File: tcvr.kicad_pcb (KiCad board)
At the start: 2 copper layers, 51 parts, among them J1 9V 43-04-70, J2 anterna 50 Ohm, J3 jack 43-08-39, J4 hole, Q1 BC817 86-05-47, Q2 2N7002, Q3 PZT2222A 86-02-43, SW1 SW_DPST_x2, U1 LM386 89-24-08, Y1 3579kHz 40-00-62

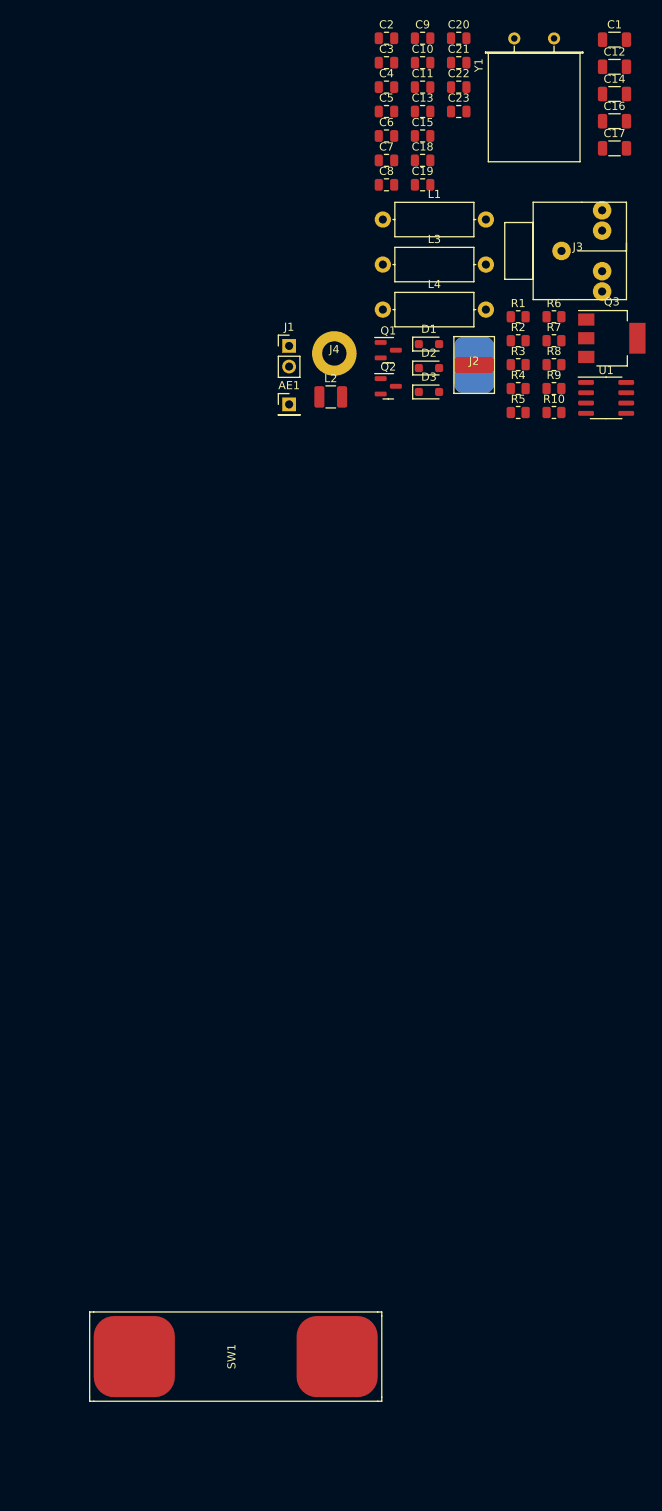
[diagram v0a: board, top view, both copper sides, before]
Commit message: made pcb placment
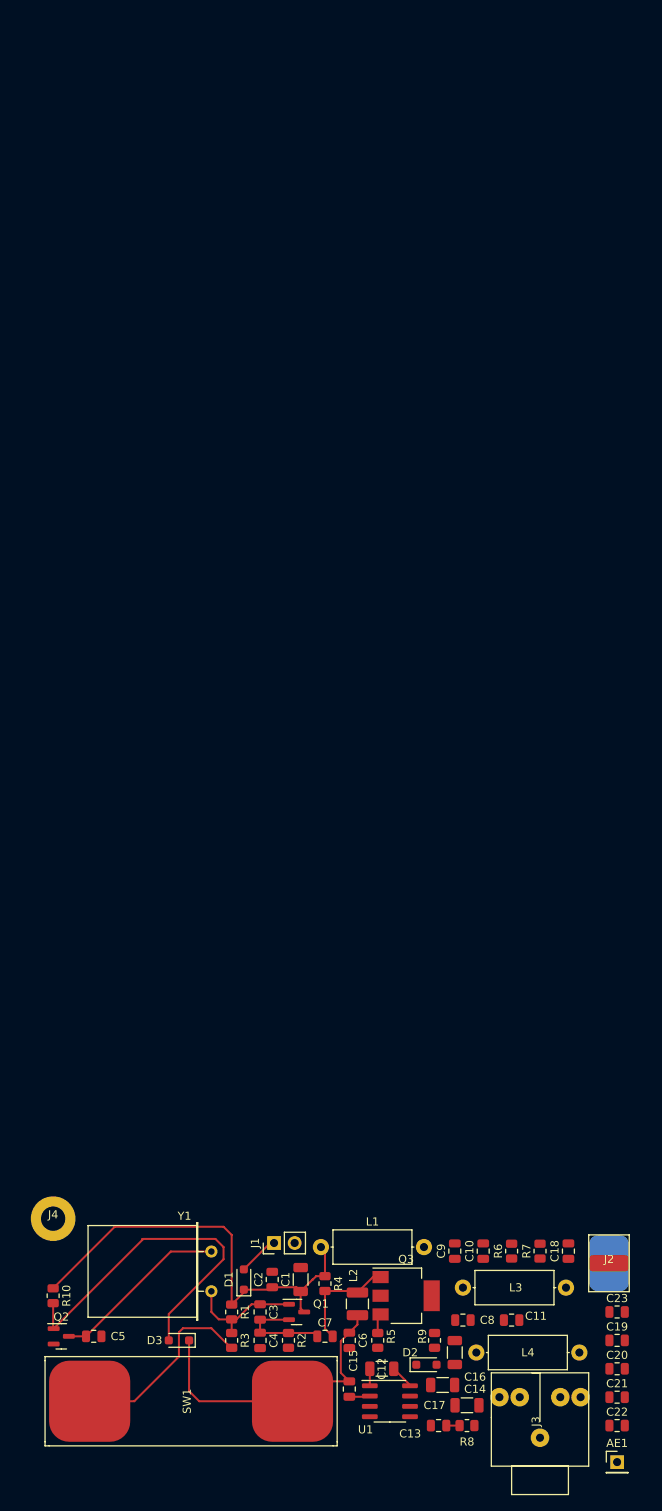
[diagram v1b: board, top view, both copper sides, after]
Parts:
- moved C22 166.1 mm to (147.5, 113.5)
- moved C21 165.6 mm to (147.5, 110.0)
- moved C20 165.1 mm to (147.5, 106.5)
- moved C12 163.0 mm to (118.5, 106.5), turned to 180 degrees
- moved C13 162.0 mm to (125.5, 113.5)
- moved C14 160.5 mm to (126.0, 108.5)
- moved C1 157.6 mm to (108.5, 95.5), turned to 90 degrees
- moved C17 156.0 mm to (129.0, 111.0)
- moved C4 155.2 mm to (103.5, 103.0), turned to -90 degrees
- moved C5 155.2 mm to (83.0, 102.5)
- moved C3 154.7 mm to (103.5, 99.5), turned to -90 degrees
- moved C15 154.7 mm to (114.5, 109.0), turned to 90 degrees
- moved Y1 154.1 mm to (97.5, 92.0), turned to -90 degrees
- moved C2 153.6 mm to (105.0, 95.5), turned to 90 degrees
- moved C16 153.0 mm to (127.5, 104.5), turned to 90 degrees
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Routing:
- net Net-(D1-K): track 0.00 -> 54.2 mm
- net Net-(D3-A): track 0.00 -> 43.5 mm
- net Net-(D2-K): track 0.00 -> 39.4 mm
- net GND: track 0.00 -> 24.0 mm
- net Net-(Q2-D): track 0.00 -> 21.9 mm
- net Net-(Q1-B): track 0.00 -> 14.9 mm
- net Net-(Q3-B): track 0.00 -> 13.7 mm
- net Net-(Q1-E): track 0.00 -> 12.4 mm
- net Net-(D1-A): track 0.00 -> 5.07 mm
- net Net-(C12-Pad1): track 0.00 -> 2.92 mm
- net Net-(U1--): track 0.00 -> 2.56 mm
- net Net-(C12-Pad2): track 0.00 -> 2.09 mm
- net Net-(C13-Pad2): track 0.00 -> 1.64 mm

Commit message: made pcb design
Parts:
- moved J4 2.50 mm to (78.0, 90.5)
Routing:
- net GND: track 24.0 -> 88.7 mm
- net Net-(J2-Pin_1): track 0.00 -> 35.8 mm
- net Net-(AE1-A): track 0.00 -> 23.2 mm
- net Net-(D1-K): track 54.2 -> 76.4 mm
- net Net-(D2-A): track 0.00 -> 13.4 mm
- net Net-(J3-Pin_1): track 0.00 -> 12.9 mm
- net Net-(C11-Pad1): track 0.00 -> 12.5 mm
- net Net-(Q3-C): track 0.00 -> 10.6 mm
- net Net-(D2-K): track 39.4 -> 49.1 mm
- net Net-(C13-Pad1): track 0.00 -> 7.04 mm
- net Net-(U1-BYPASS): track 0.00 -> 3.12 mm
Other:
- board outline added: 77 x 35.5 mm

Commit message: pcb finished
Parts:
- moved C12 0.50 mm to (118.5, 106.0)
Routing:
- added copper zone on B.Cu, net GND
- added copper zone on F.Cu, net GND
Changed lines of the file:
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@@
   (setup
     (pad_to_mask_clearance 0)
+    (aux_axis_origin 73.5 121.5)
+    (grid_origin 73.5 121.5)
     (pcbplotparams
       (layerselection 0x00010fc_ffffffff)
@@
     (property "ki_keywords" "cap capacitor")
     (attr smd)
-    (fp_text reference "C15" (at 3.5 0.5 90) (layer "F.SilkS")
+    (fp_text reference "C15" (at 3 0 90) (layer "F.SilkS")
         (effects (font (size 1 1) (thickness 0.15)))
     )
@@
     (property "ki_keywords" "NPN General Puprose Transistor SMD")
     (attr smd)
-    (fp_text reference "Q3" (at 0 -4.5) (layer "F.SilkS")
+    (fp_text reference "Q3" (at 0 0) (layer "F.SilkS")
         (effects (font (size 1 1) (thickness 0.15)))
     )
@@
     (property "ki_keywords" "diode Schottky")
     (attr smd)
-    (fp_text reference "D2" (at -2 -1.5) (layer "F.SilkS")
+    (fp_text reference "D2" (at -1 -2) (layer "F.SilkS")
         (effects (font (size 1 1) (thickness 0.15)))
     )
@@
   )
   (footprint "Capacitor_SMD:C_1206_3216Metric" (layer "F.Cu")
-    (at 118.5 106.5 180)
+    (at 118.5 106 180)
     (descr "Capacitor SMD 1206 (3216 Metric), square (rectangular) end terminal, IPC_7351 nominal, (Body size source: IPC-SM-782 page 76, https://www.pcb-3d.com/wordpress/wp-content/uploads/ipc-sm-782a_amendment_1_and_2.pdf), generated with kicad-footprint-generator")
     (tags "capacitor")
@@
     (property "ki_keywords" "cap capacitor")
     (attr smd)
-    (fp_text reference "C12" (at 0 0 90) (layer "F.SilkS")
+    (fp_text reference "C12" (at -2 2 180) (layer "F.SilkS")
         (effects (font (size 1 1) (thickness 0.15)))
     )
@@
   (segment (start 134.5 92.9125) (end 138 92.9125) (width 0.25) (layer "F.Cu") (net 5))
   (segment (start 135.45 100.5) (end 131.45 104.5) (width 0.25) (layer "F.Cu") (net 5))
-  (segment (start 145.95 92.95) (end 141.5 92.95) (width 0.25) (layer "F.Cu") (net 5))
   (segment (start 135.45 100.5) (end 135.45 97.4) (width 0.25) (layer "F.Cu") (net 5))
-  (segment (start 146.5 93.5) (end 145.95 92.95) (width 0.25) (layer "F.Cu") (net 5))
+  (segment (start 146.5 93.5) (end 142.05 93.5) (width 0.25) (layer "F.Cu") (net 5))
   (segment (start 131 92.95) (end 134.4625 92.95) (width 0.25) (layer "F.Cu") (net 5))
   (segment (start 141.4625 92.9125) (end 141.5 92.95) (width 0.25) (layer "F.Cu") (net 5))
@@
   (segment (start 141.5 96.2) (end 141.2 96.5) (width 0.25) (layer "F.Cu") (net 5))
   (segment (start 131.45 104.5) (end 130.15 104.5) (width 0.25) (layer "F.Cu") (net 5))
+  (segment (start 142.05 93.5) (end 141.5 92.95) (width 0.25) (layer "F.Cu") (net 5))
   (segment (start 120 91.5) (end 111 91.5) (width 0.25) (layer "F.Cu") (net 6))
   (segment (start 100 90) (end 99 89) (width 0.25) (layer "F.Cu") (net 6))
@@
   (segment (start 101.5 94.25) (end 104.75 91) (width 0.25) (layer "F.Cu") (net 22))
   (segment (start 104.75 91) (end 105.225 91) (width 0.25) (layer "F.Cu") (net 22))
+  (zone (net 1) (net_name "GND") (layer "F.Cu") (hatch edge 0.5)
+    (connect_pads (clearance 0.5))
+    (min_thickness 0.25) (filled_areas_thickness no)
+    (fill yes (thermal_gap 0.5) (thermal_bridge_width 0.5))
+    (polygon
+      (pts
+        (xy 150.5 86)
+        (xy 150.5 121.5)
+        (xy 73.5 121.5)
+        (xy 73.5 86)
+      )
+    )
+  )
+  (zone (net 1) (net_name "GND") (layer "B.Cu") (hatch edge 0.5)
+    (priority 1)
+    (connect_pads (clearance 0.5))
+    (min_thickness 0.25) (filled_areas_thickness no)
+    (fill yes (thermal_gap 0.5) (thermal_bridge_width 0.5))
+    (polygon
+      (pts
+        (xy 150.5 86)
+        (xy 150.5 121.5)
+        (xy 73.5 121.5)
+        (xy 73.5 86)
+      )
+    )
+  )
 )

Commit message: added name
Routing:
- net Net-(Q1-E): track 12.4 -> 10.5 mm
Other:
- board text added: "garobcsi"

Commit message: updated pcb
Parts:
- moved C6 1.00 mm to (115.5, 103.0)
- moved C7 1.00 mm to (110.5, 102.5)
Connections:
- J4 pad 1: unconnected-(J4-Pin_1-Pad1) -> GND
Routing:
- net GND: track 88.7 -> 85.3 mm
- net Net-(Q1-E): track 10.5 -> 9.50 mm
- net Net-(D2-K): track 49.1 -> 49.7 mm
